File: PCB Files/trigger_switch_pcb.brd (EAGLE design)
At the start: 100 x 80 mm, 7 parts

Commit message: update to wiring diagram
i think i have the board schematic done!   All grounds on the bottom,
all signals on the top
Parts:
- moved JP1 72.7 mm to (101.6, 80.0)
- moved JP2 11.7 mm to (29.2, 19.1)
- moved SV1 6.48 mm to (100.3, 41.9)
- moved U$1 5.24 mm to (54.6, 59.7)
- moved R1 3.81 mm to (39.4, 35.6), turned to 180 degrees
- moved JP3 1.80 mm to (21.6, 19.1)
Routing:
- net GND: track 35.7 -> 247.8 mm
- net TRIG: track 0.00 -> 64.3 mm
- net V1: track 0.00 -> 61.1 mm
- net V2: track 0.00 -> 57.5 mm
- net V3: track 0.00 -> 53.9 mm
- net V4: track 0.00 -> 50.3 mm
- net V5: track 0.00 -> 46.7 mm
- net V16: track 0.00 -> 46.4 mm
- net V15: track 0.00 -> 43.9 mm
- net V6: track 0.00 -> 43.1 mm
- net V14: track 0.00 -> 41.3 mm
- net V7: track 0.00 -> 39.6 mm
- net V13: track 0.00 -> 38.8 mm
- net V12: track 0.00 -> 36.3 mm
- net V8: track 0.00 -> 36.0 mm
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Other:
- board size 100 x 80 mm -> 120.3 x 95.2 mm
- board text added: "Trigger Swticher Andrew Giessel 2013"

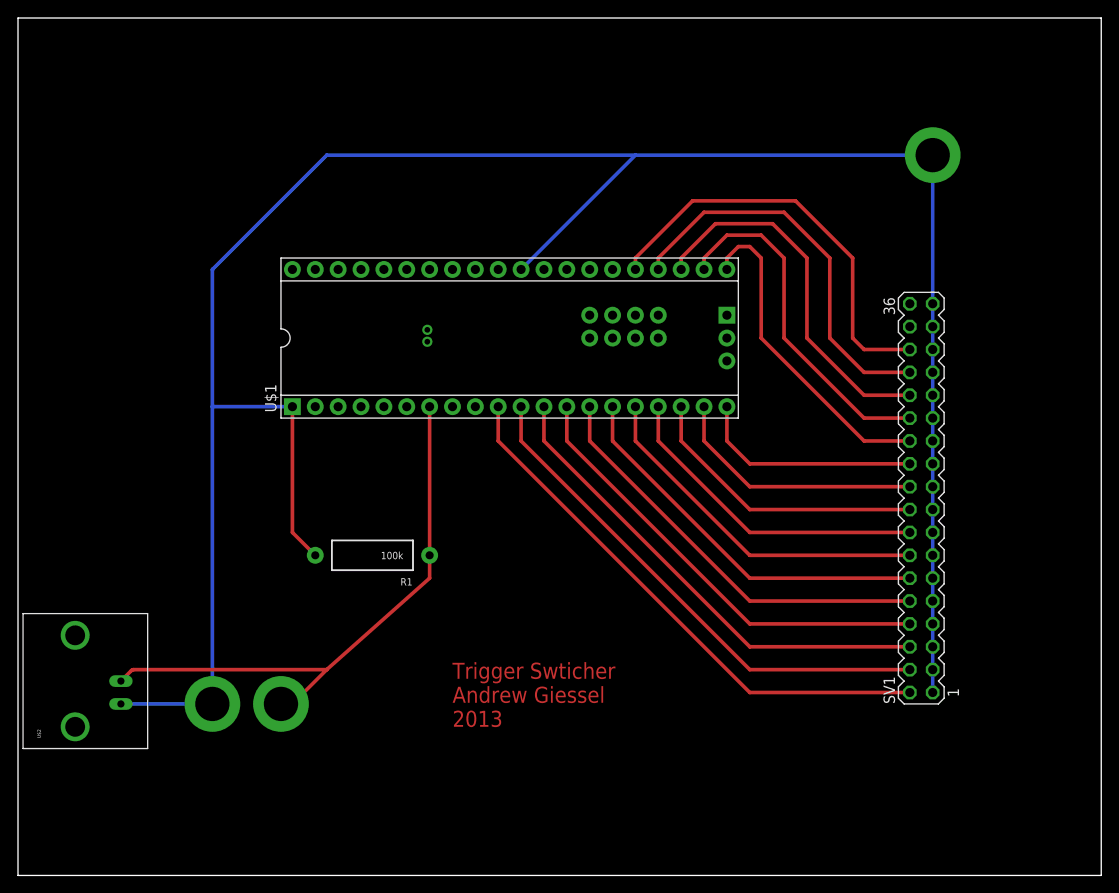
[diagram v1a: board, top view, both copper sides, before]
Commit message: Final? Changes to board
added standoffs, resized board
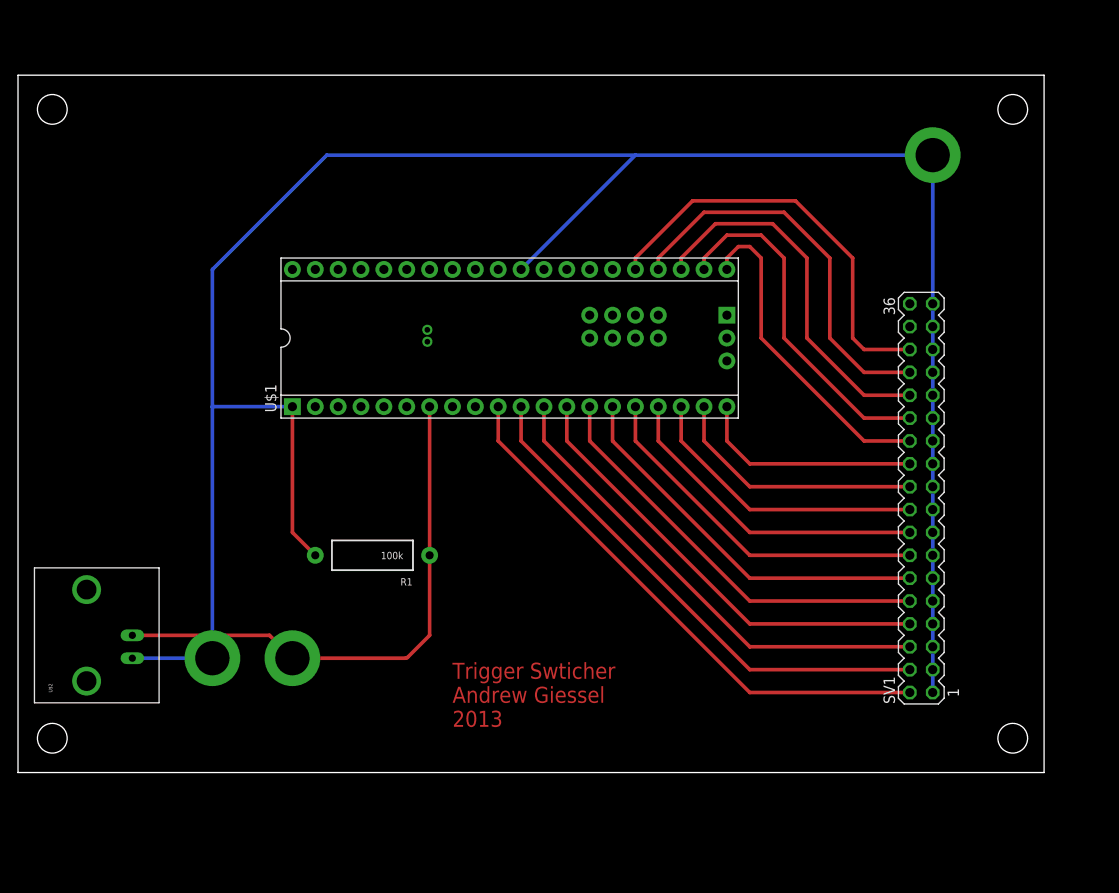
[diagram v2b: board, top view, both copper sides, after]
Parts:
- added U$3, U$4, U$5, U$6: (no value), SparkFun-Electromechanical:STAND-OFF
- moved U$2 5.24 mm to (12.7, 26.7)
- moved JP2 5.24 mm to (30.5, 24.1)
- moved JP3 5.08 mm to (21.6, 24.1)
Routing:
- net GND: track 247.8 -> 241.4 mm
- net TRIG: track 64.3 -> 60.5 mm
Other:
- board size 120.3 x 95.2 mm -> 114 x 77.5 mm
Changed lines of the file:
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@@
 <board>
 <plain>
-<wire x1="0" y1="0" x2="120.32" y2="0" width="0" layer="20"/>
-<wire x1="120.32" y1="0" x2="120.32" y2="95.24" width="0" layer="20"/>
-<wire x1="120.32" y1="95.24" x2="0" y2="95.24" width="0" layer="20"/>
-<wire x1="0" y1="95.24" x2="0" y2="0" width="0" layer="20"/>
+<wire x1="0" y1="11.43" x2="113.97" y2="11.43" width="0" layer="20"/>
+<wire x1="113.97" y1="11.43" x2="113.97" y2="88.89" width="0" layer="20"/>
+<wire x1="113.97" y1="88.89" x2="0" y2="88.89" width="0" layer="20"/>
+<wire x1="0" y1="88.89" x2="0" y2="11.43" width="0" layer="20"/>
 <text x="48.26" y="16.51" size="1.778" layer="1">Trigger Swticher
 Andrew Giessel
@@
 <element name="U$1" library="teensypp" package="TEENSY++" value="ARDUINO-TEENSY++" x="54.61" y="59.69"/>
 <element name="R1" library="SparkFun-Resistors" package="AXIAL-0.5" value="100k" x="39.37" y="35.56" rot="R180"/>
-<element name="U$2" library="SparkFun-Connectors" package="BNC" value="BNCPTH" x="11.43" y="21.59" rot="R90"/>
+<element name="U$2" library="SparkFun-Connectors" package="BNC" value="BNCPTH" x="12.7" y="26.67" rot="R90"/>
 <element name="SV1" library="con-lstb" package="MA18-2" value="" x="100.33" y="41.91" rot="R90">
 <attribute name="OC_NEWARK" value="unknown" x="172.72" y="78.74" size="1.778" layer="27" rot="R90" display="off"/>
@@
 </element>
 <element name="JP1" library="SparkFun-Connectors" package="SMTSO-256-ET" value="M01-SMTSO-256-ET" x="101.6" y="80.01"/>
-<element name="JP2" library="SparkFun-Connectors" package="SMTSO-256-ET" value="M01-SMTSO-256-ET" x="29.21" y="19.05"/>
-<element name="JP3" library="SparkFun-Connectors" package="SMTSO-256-ET" value="M01-SMTSO-256-ET" x="21.59" y="19.05"/>
+<element name="JP2" library="SparkFun-Connectors" package="SMTSO-256-ET" value="M01-SMTSO-256-ET" x="30.48" y="24.13"/>
+<element name="JP3" library="SparkFun-Connectors" package="SMTSO-256-ET" value="M01-SMTSO-256-ET" x="21.59" y="24.13"/>
+<element name="U$3" library="SparkFun-Electromechanical" package="STAND-OFF" value="" x="3.81" y="85.09"/>
+<element name="U$4" library="SparkFun-Electromechanical" package="STAND-OFF" value="" x="110.49" y="85.09"/>
+<element name="U$5" library="SparkFun-Electromechanical" package="STAND-OFF" value="" x="110.49" y="15.24"/>
+<element name="U$6" library="SparkFun-Electromechanical" package="STAND-OFF" value="" x="3.81" y="15.24"/>
 </elements>
 <signals>
@@
 <contactref element="U$2" pad="GND"/>
 <contactref element="U$1" pad="GND"/>
-<wire x1="11.43" y1="19.05" x2="21.59" y2="19.05" width="0.4064" layer="16"/>
+<wire x1="12.7" y1="24.13" x2="21.59" y2="24.13" width="0.4064" layer="16"/>
 <wire x1="101.6" y1="80.01" x2="68.58" y2="80.01" width="0.4064" layer="16"/>
 <wire x1="68.58" y1="80.01" x2="34.29" y2="80.01" width="0.4064" layer="16"/>
 <wire x1="34.29" y1="80.01" x2="21.59" y2="67.31" width="0.4064" layer="16"/>
 <wire x1="21.59" y1="67.31" x2="21.59" y2="52.07" width="0.4064" layer="16"/>
-<wire x1="21.59" y1="52.07" x2="21.59" y2="19.05" width="0.4064" layer="16"/>
+<wire x1="21.59" y1="52.07" x2="21.59" y2="24.13" width="0.4064" layer="16"/>
 <wire x1="55.88" y1="67.31" x2="68.58" y2="80.01" width="0.4064" layer="16"/>
 <wire x1="30.48" y1="52.07" x2="21.59" y2="52.07" width="0.4064" layer="16"/>
@@
 <contactref element="U$1" pad="D4"/>
 <wire x1="45.72" y1="35.56" x2="45.72" y2="52.07" width="0.4064" layer="1"/>
-<wire x1="45.72" y1="33.02" x2="45.72" y2="35.56" width="0.4064" layer="1"/>
-<wire x1="11.43" y1="21.59" x2="12.60700625" y2="22.76700625" width="0.4064" layer="1"/>
-<wire x1="12.60700625" y1="22.76700625" x2="12.8315125" y2="22.86" width="0.4064" layer="1" curve="-45"/>
-<wire x1="12.8315125" y1="22.86" x2="34.29" y2="22.86" width="0.4064" layer="1"/>
-<wire x1="34.29" y1="22.86" x2="45.72" y2="33.02" width="0.4064" layer="1"/>
-<wire x1="29.21" y1="19.05" x2="30.3484875" y2="19.05" width="0.4064" layer="1"/>
-<wire x1="30.3484875" y1="19.05" x2="30.57299375" y2="19.14299375" width="0.4064" layer="1" curve="45"/>
-<wire x1="30.57299375" y1="19.14299375" x2="34.29" y2="22.86" width="0.4064" layer="1"/>
+<wire x1="12.7" y1="26.67" x2="27.94" y2="26.67" width="0.4064" layer="1"/>
+<wire x1="27.94" y1="26.67" x2="30.48" y2="24.13" width="0.4064" layer="1"/>
+<wire x1="30.48" y1="24.13" x2="43.0484875" y2="24.13" width="0.4064" layer="1"/>
+<wire x1="43.0484875" y1="24.13" x2="43.27299375" y2="24.22299375" width="0.4064" layer="1" curve="45"/>
+<wire x1="43.27299375" y1="24.22299375" x2="45.72" y2="26.67" width="0.4064" layer="1"/>
+<wire x1="45.72" y1="26.67" x2="45.72" y2="35.56" width="0.4064" layer="1"/>
 </signal>
 <signal name="V6">
